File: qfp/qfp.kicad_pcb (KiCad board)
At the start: 2 copper layers, 4 parts, among them P1 CONN_01X24, P2 CONN_01X24, U1 QFP48, U2 TQFP48

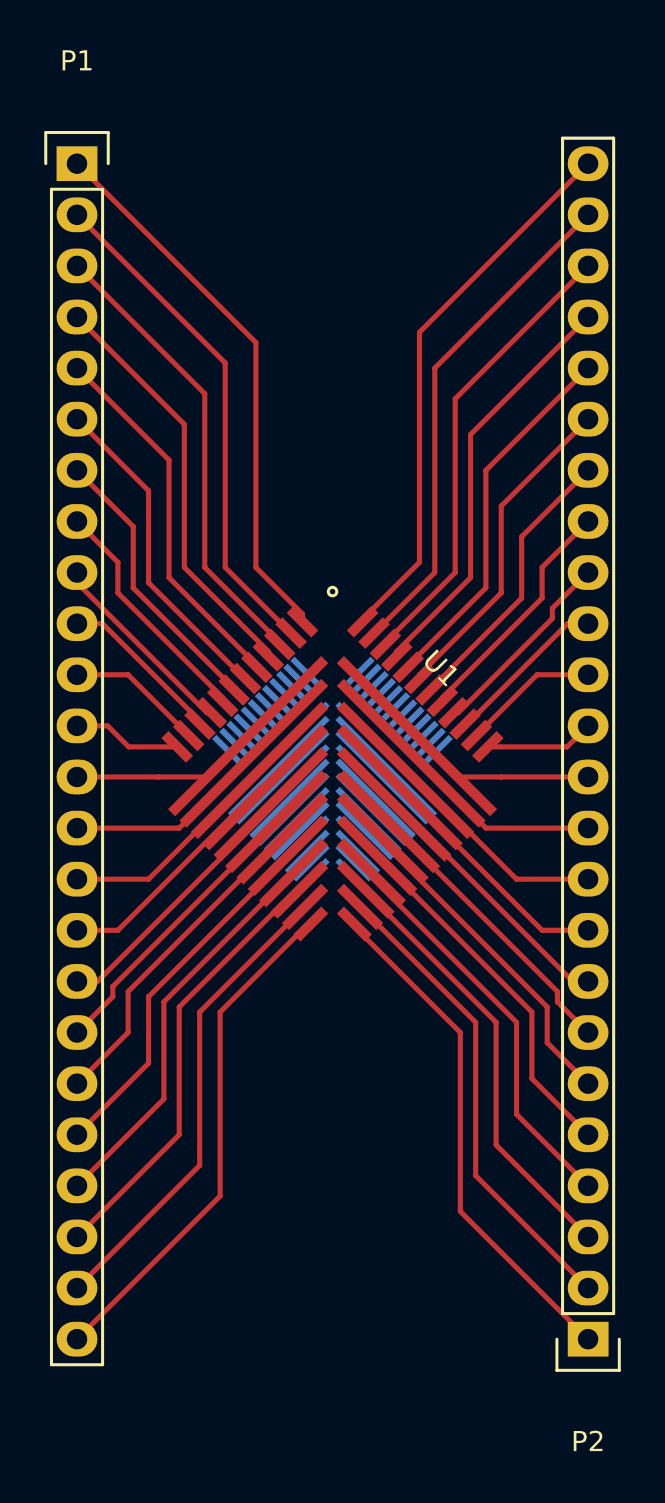
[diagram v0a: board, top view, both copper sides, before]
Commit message: Route the 0.5mm-pitch QFP side.
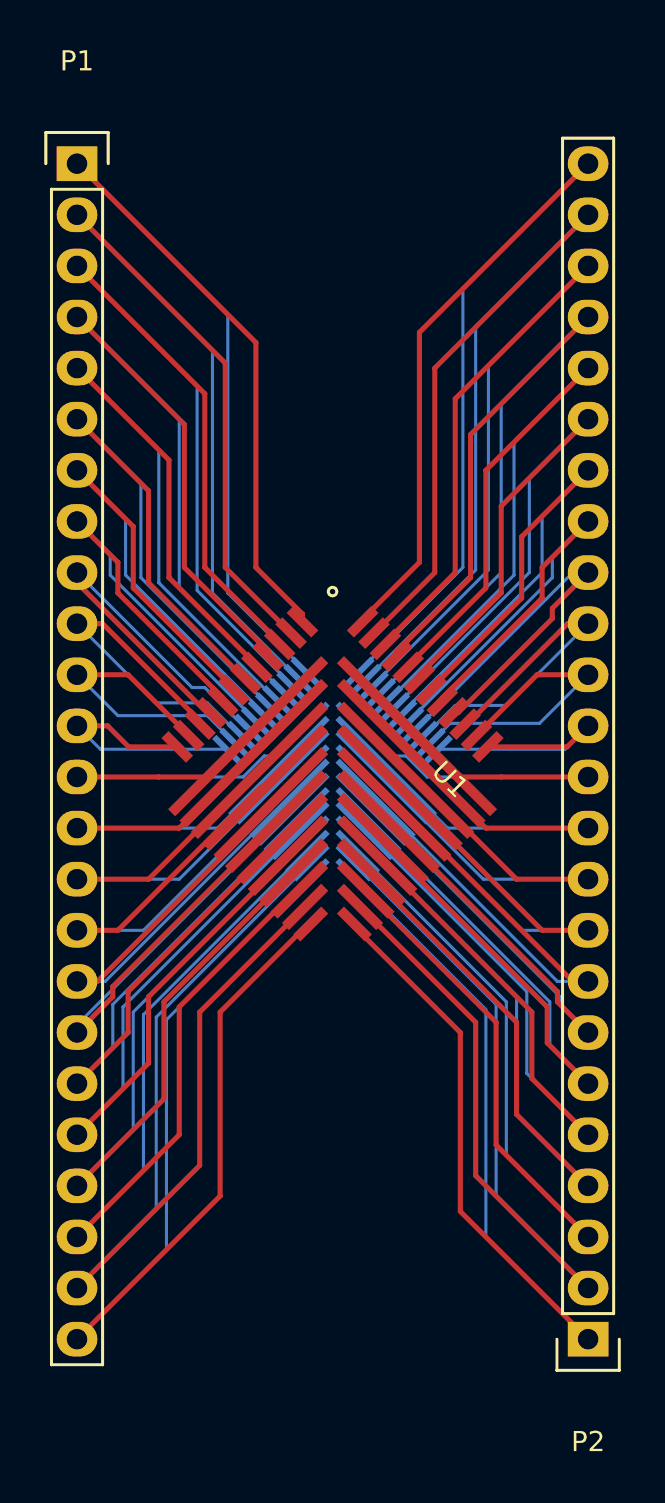
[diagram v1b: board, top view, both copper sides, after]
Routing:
- net PIN1: track 27.4 -> 57.3 mm
- net PIN48: track 27.4 -> 57.3 mm
- net PIN24: track 25.5 -> 53.6 mm
- net PIN25: track 25.4 -> 53.5 mm
- net PIN47: track 25.2 -> 52.8 mm
- net PIN2: track 25.2 -> 52.8 mm
- net PIN26: track 23.6 -> 49.6 mm
- net PIN23: track 23.6 -> 49.6 mm
- net PIN46: track 23.0 -> 48.2 mm
- net PIN3: track 23.0 -> 48.2 mm
- net PIN22: track 21.9 -> 45.8 mm
- net PIN27: track 21.8 -> 45.7 mm
- net PIN4: track 20.8 -> 43.7 mm
- net PIN45: track 20.8 -> 43.7 mm
- net PIN21: track 20.0 -> 41.8 mm
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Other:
- net class Default: clearance 0.254 -> 0.1524
- rule trace_clearance: 0.254 -> 0.1524
- rule trace_min: 0.254 -> 0.1524

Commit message: Add silkscreen labels.
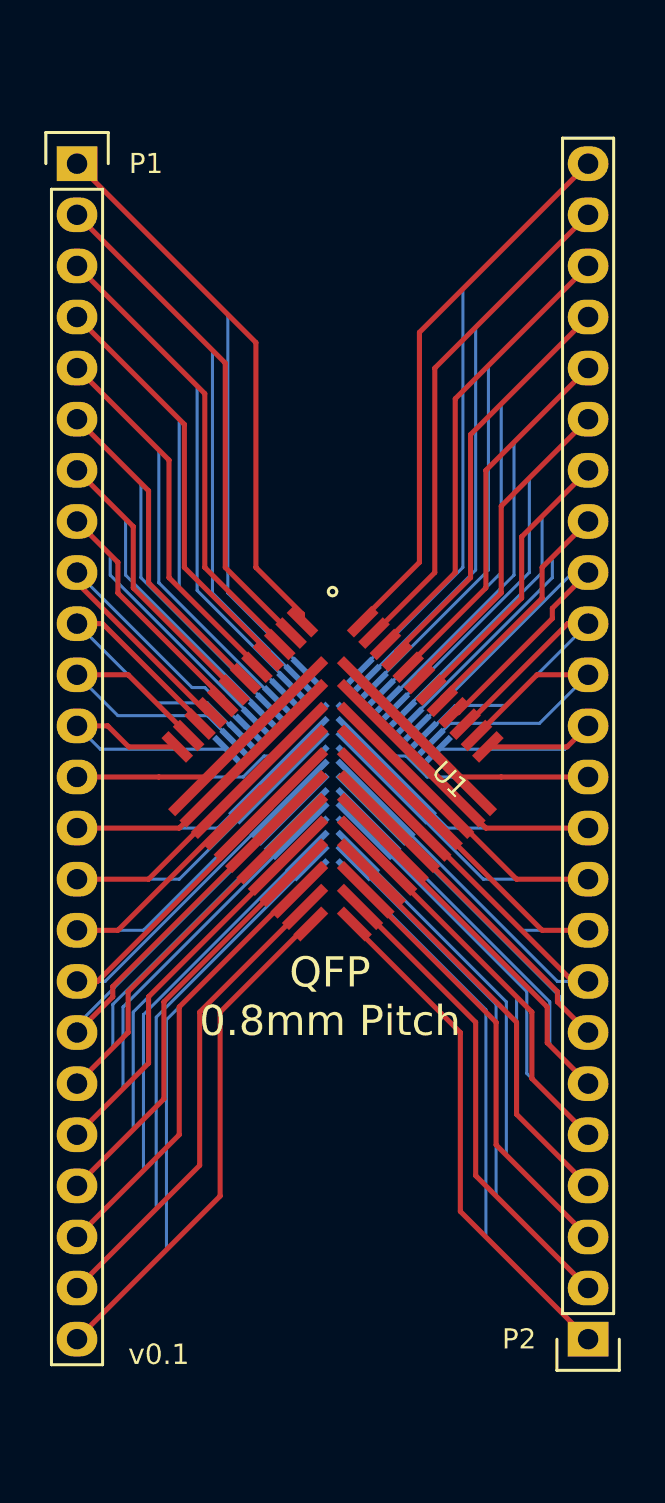
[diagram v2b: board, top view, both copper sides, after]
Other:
- board text added: "QFP 0.5mm Pitch"
- board text added: "QFP 0.8mm Pitch"
- board text added: "v0.1"
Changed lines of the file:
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@@
     (area 129.457667 83.891 170.262334 150.649001)
     (thickness 1.6)
-    (drawings 0)
+    (drawings 3)
     (tracks 353)
     (zones 0)
@@
   (page A4)
   (layers
-    (0 F.Cu signal hide)
+    (0 F.Cu signal)
     (31 B.Cu signal)
     (32 B.Adhes user)
@@
     (pad_to_mask_clearance 0)
     (aux_axis_origin 0 0)
-    (visible_elements FFFFFD7F)
+    (visible_elements FFFFFF7F)
     (pcbplotparams
       (layerselection 0x00030_80000001)
@@
     (descr "Through hole pin header")
     (tags "pin header")
-    (fp_text reference P1 (at 0 -5.1) (layer F.SilkS)
+    (fp_text reference P1 (at 3.429 0) (layer F.SilkS)
       (effects (font (size 1 1) (thickness 0.15)))
     )
@@
     (descr "Through hole pin header")
     (tags "pin header")
-    (fp_text reference P2 (at 0 -5.1 180) (layer F.SilkS)
+    (fp_text reference P2 (at 3.429 0 180) (layer F.SilkS)
       (effects (font (size 1 1) (thickness 0.15)))
     )
@@
       (net 1 PIN1))
   )
+  (gr_text v0.1 (at 141.224 148.082) (layer F.SilkS)
+    (effects (font (size 1.016 1.016) (thickness 0.0635)))
+  )
+  (gr_text "QFP\n0.5mm Pitch" (at 149.733 130.302) (layer B.SilkS)
+    (effects (font (size 1.5 1.5) (thickness 0.3)) (justify mirror))
+  )
+  (gr_text "QFP\n0.8mm Pitch" (at 149.733 130.302) (layer F.SilkS)
+    (effects (font (size 1.5 1.5) (thickness 0.3)))
+  )
   (segment (start 148.481142 114.112054) (end 148.481142 114.064142) (width 0.1524) (layer B.Cu) (net 1))

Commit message: Board outline
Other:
- board outline added: 29 x 62.1 mm
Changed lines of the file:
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@@
     (links 96)
     (no_connects 0)
-    (area 129.457667 83.891 170.262334 150.649001)
+    (area 135.331999 86.944999 164.388001 149.148001)
     (thickness 1.6)
-    (drawings 3)
+    (drawings 7)
     (tracks 353)
     (zones 0)
@@
   (module smdproto:PROTOQFP (layer F.Cu)
     (at 149.86 119.38 315)
-    (fp_text reference U1 (at 4.22072 -4.041115 315) (layer F.SilkS)
+    (fp_text reference U1 (at 5.926969 -5.926969 315) (layer F.SilkS)
       (effects (font (size 1 1) (thickness 0.15)))
     )
@@
       (net 1 PIN1))
   )
+  (gr_line (start 135.382 86.995) (end 135.382 149.098) (angle 90) (layer Edge.Cuts) (width 0.1))
+  (gr_line (start 164.338 86.995) (end 135.382 86.995) (angle 90) (layer Edge.Cuts) (width 0.1))
+  (gr_line (start 164.338 149.098) (end 164.338 86.995) (angle 90) (layer Edge.Cuts) (width 0.1))
+  (gr_line (start 135.382 149.098) (end 164.338 149.098) (angle 90) (layer Edge.Cuts) (width 0.1))
   (gr_text v0.1 (at 141.224 148.082) (layer F.SilkS)
     (effects (font (size 1.016 1.016) (thickness 0.0635)))
